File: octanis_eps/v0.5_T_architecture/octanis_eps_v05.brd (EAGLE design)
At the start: 80 x 50 mm, 141 parts, among them IC1 OPA2333DGK, Q3 32.768kHz, Q4 BSS123, U1 BQ24650_RVA_16, U10 CSD16327Q3_DQG_8, U13 CSD16327Q3_DQG_8, U14 CSD16327Q3_DQG_8, U2 Value, U3 Value, U4 Value, U5 TPS2022D, U6 TPS61232, U7 CSD16327Q3_DQG_8, U8 MSP430G2544, U9 CSD16327Q3_DQG_8

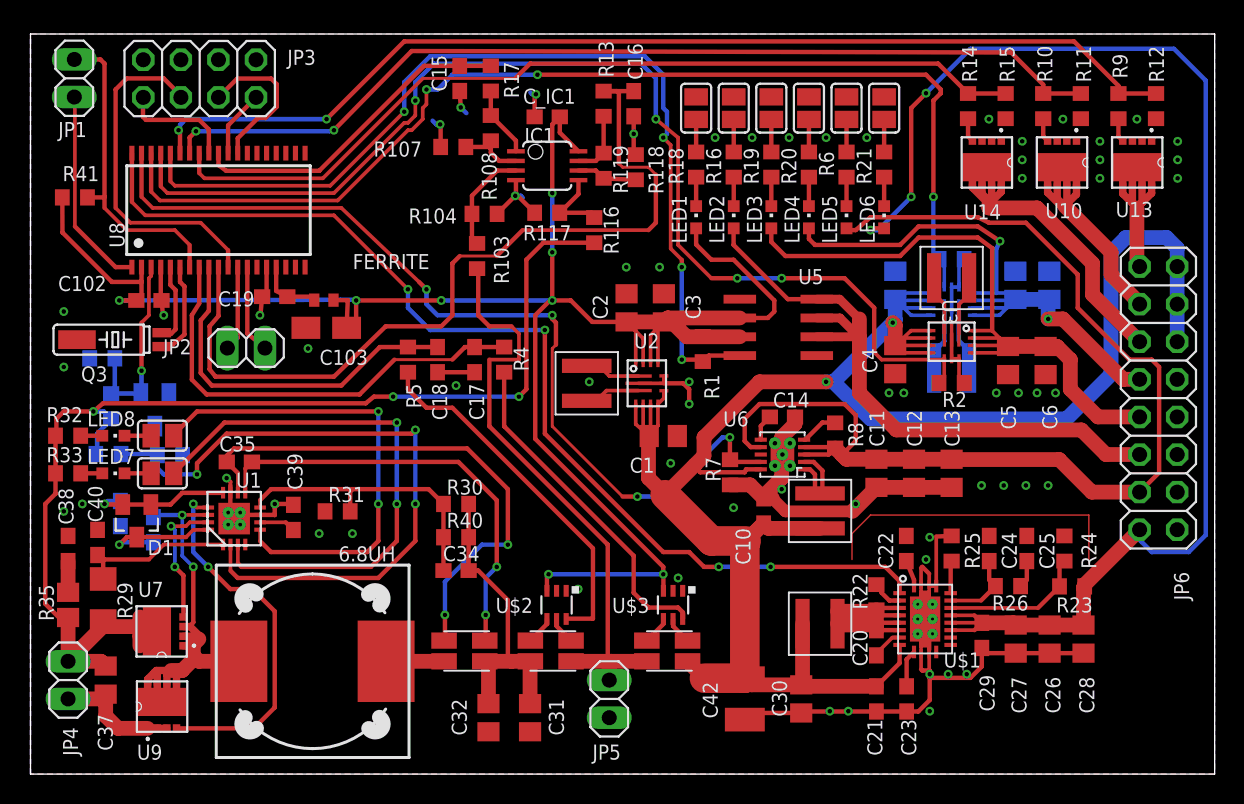
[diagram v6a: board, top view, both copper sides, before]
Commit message: Added mounting holes and header names
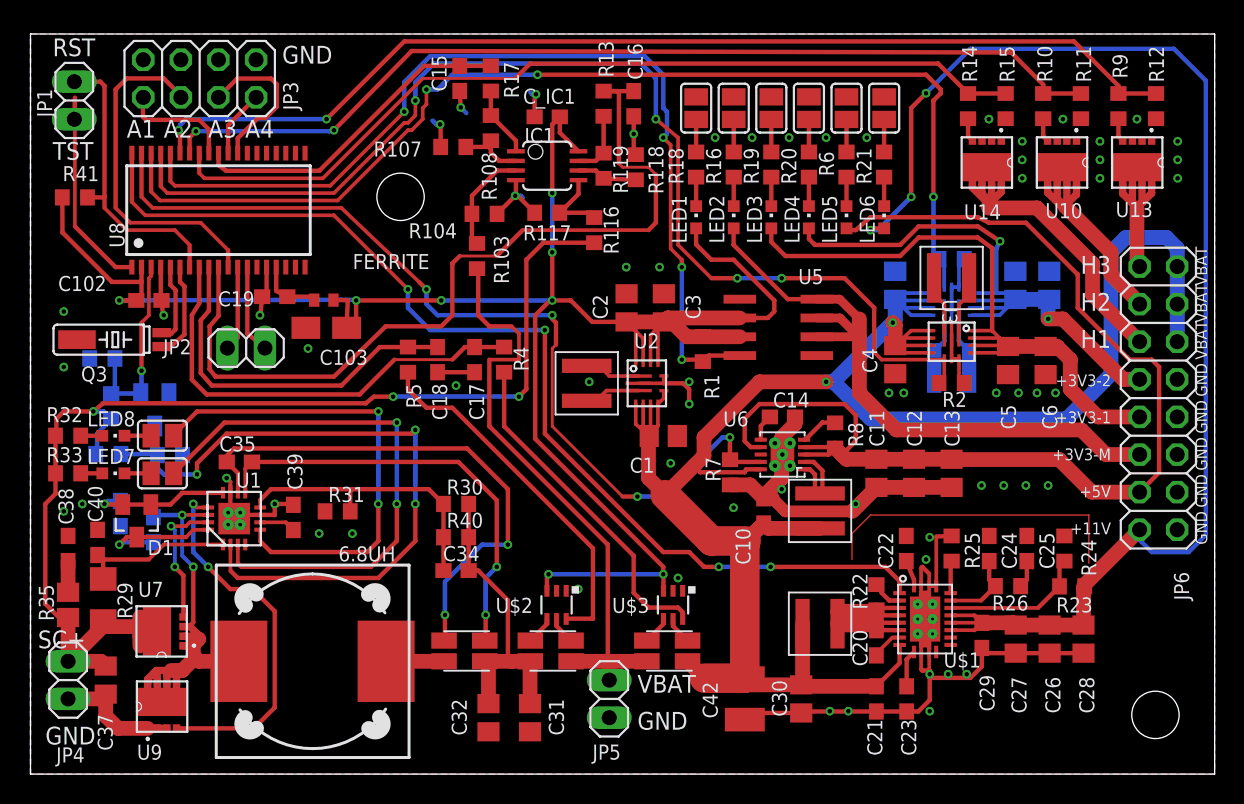
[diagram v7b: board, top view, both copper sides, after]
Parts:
- moved JP1 1.50 mm to (2.96, 45.5)
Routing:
- net N$93: track 21.4 -> 19.9 mm
- net N$75: track 13.7 -> 15.1 mm
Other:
- board text added: "+11V"
- board text added: "+3V3-1"
- board text added: "+3V3-2"
- board text added: "+3V3-M"
- board text added: "+5V"
- board text added: "A1"
- board text added: "A2"
- board text added: "A3"
- board text added: "A4"
- board text added: "GND"
- board text added: "H1"
- board text added: "H2"
- board text added: "H3"
- board text added: "RST"
- board text added: "SC+"
- board text added: "TST"
- board text added: "VBAT"
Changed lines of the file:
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@@
 <setting verticaltext="up"/>
 </settings>
-<grid distance="0.1" unitdist="mm" unit="mm" style="lines" multiple="1" display="no" altdistance="0.025" altunitdist="inch" altunit="inch"/>
+<grid distance="0.5" unitdist="mm" unit="mm" style="lines" multiple="1" display="no" altdistance="0.025" altunitdist="inch" altunit="inch"/>
 <layers>
 <layer number="1" name="Top" color="4" fill="1" visible="yes" active="yes"/>
@@
 <layer number="22" name="bPlace" color="7" fill="1" visible="yes" active="yes"/>
 <layer number="23" name="tOrigins" color="15" fill="1" visible="yes" active="yes"/>
-<layer number="24" name="bOrigins" color="15" fill="1" visible="no" active="yes"/>
+<layer number="24" name="bOrigins" color="15" fill="1" visible="yes" active="yes"/>
 <layer number="25" name="tNames" color="7" fill="1" visible="yes" active="yes"/>
-<layer number="26" name="bNames" color="7" fill="1" visible="no" active="yes"/>
+<layer number="26" name="bNames" color="7" fill="1" visible="yes" active="yes"/>
 <layer number="27" name="tValues" color="7" fill="1" visible="no" active="yes"/>
-<layer number="28" name="bValues" color="7" fill="1" visible="no" active="yes"/>
+<layer number="28" name="bValues" color="7" fill="1" visible="yes" active="yes"/>
 <layer number="29" name="tStop" color="7" fill="3" visible="no" active="yes"/>
 <layer number="30" name="bStop" color="7" fill="6" visible="no" active="yes"/>
@@
 <layer number="42" name="bRestrict" color="1" fill="10" visible="no" active="yes"/>
 <layer number="43" name="vRestrict" color="2" fill="10" visible="no" active="yes"/>
-<layer number="44" name="Drills" color="7" fill="1" visible="no" active="yes"/>
-<layer number="45" name="Holes" color="7" fill="1" visible="no" active="yes"/>
+<layer number="44" name="Drills" color="7" fill="1" visible="yes" active="yes"/>
+<layer number="45" name="Holes" color="7" fill="1" visible="yes" active="yes"/>
 <layer number="46" name="Milling" color="3" fill="1" visible="no" active="yes"/>
 <layer number="47" name="Measures" color="7" fill="1" visible="no" active="yes"/>
@@
 <layer number="50" name="dxf" color="7" fill="1" visible="no" active="no"/>
 <layer number="51" name="tDocu" color="7" fill="1" visible="yes" active="yes"/>
-<layer number="52" name="bDocu" color="7" fill="1" visible="no" active="yes"/>
+<layer number="52" name="bDocu" color="7" fill="1" visible="yes" active="yes"/>
 <layer number="53" name="tGND_GNDA" color="7" fill="9" visible="no" active="no"/>
 <layer number="54" name="bGND_GNDA" color="1" fill="9" visible="no" active="no"/>
@@
 <wire x1="80" y1="50" x2="0" y2="50" width="0" layer="20"/>
 <wire x1="0" y1="50" x2="0" y2="0" width="0" layer="20"/>
+<hole x="25" y="39" drill="3.2"/>
+<hole x="76" y="4" drill="3.2"/>
+<text x="79.5" y="33" size="0.8" layer="25" rot="R90">VBAT</text>
+<text x="79.5" y="30.5" size="0.8" layer="25" rot="R90">VBAT</text>
+<text x="79.5" y="28" size="0.8" layer="25" rot="R90">VBAT</text>
+<text x="79.5" y="25.5" size="0.8" layer="25" rot="R90">GND</text>
+<text x="79.5" y="23" size="0.8" layer="25" rot="R90">GND</text>
+<text x="79.5" y="20.5" size="0.8" layer="25" rot="R90">GND</text>
+<text x="79.5" y="18" size="0.8" layer="25" rot="R90">GND</text>
+<text x="79.5" y="15.5" size="0.8" layer="25" rot="R90">GND</text>
+<text x="73" y="24.5" size="0.8" layer="25" rot="R180">+3V3-1</text>
+<text x="73" y="27" size="0.8" layer="25" rot="R180">+3V3-2</text>
+<text x="73" y="22" size="0.8" layer="25" rot="R180">+3V3-M</text>
+<text x="73" y="19.5" size="0.8" layer="25" rot="R180">+5V</text>
+<text x="73" y="17" size="0.8" layer="25" rot="R180">+11V</text>
+<text x="73" y="30" size="1.2" layer="25" rot="R180">H1</text>
+<text x="73" y="32.5" size="1.2" layer="25" rot="R180">H2</text>
+<text x="73" y="35" size="1.2" layer="25" rot="R180">H3</text>
+<text x="41" y="3" size="1.2" layer="25">GND</text>
+<text x="41" y="5.5" size="1.2" layer="25">VBAT</text>
+<text x="1" y="2" size="1.2" layer="25">GND</text>
+<text x="0.5" y="8.5" size="1.2" layer="25">SC+</text>
+<text x="17" y="48" size="1.2" layer="25">GND</text>
+<text x="6.5" y="43" size="1.2" layer="25">A1</text>
+<text x="9" y="43" size="1.2" layer="25">A2</text>
+<text x="12" y="43" size="1.2" layer="25">A3</text>
+<text x="14.5" y="43" size="1.2" layer="25">A4</text>
+<text x="1.5" y="41.5" size="1.2" layer="25">TST</text>
+<text x="1.5" y="48.5" size="1.2" layer="25">RST</text>
 </plain>
 <attributes>
@@
 </element>
 <element name="R104" library="rcl" package="R0603" value="100k" x="30.674" y="37.849" smashed="yes" rot="R180">
-<attribute name="NAME" x="28.809" y="38.214" size="1.016" layer="25" rot="R180"/>
+<attribute name="NAME" x="28.809" y="37.214" size="1.016" layer="25" rot="R180"/>
 <attribute name="VALUE" x="31.309" y="39.754" size="1.27" layer="27" rot="R180"/>
 </element>
@@
 </element>
 <element name="R24" library="resistor" package="R0603" value="56k" x="69.85" y="15.24" smashed="yes" rot="R270">
-<attribute name="NAME" x="72.015" y="13.875" size="1.016" layer="25" rot="R90"/>
+<attribute name="NAME" x="72.015" y="13.375" size="1.016" layer="25" rot="R90"/>
 <attribute name="VALUE" x="67.945" y="15.875" size="1.27" layer="27" rot="R270"/>
 </element>
@@
 <attribute name="VALUE" x="63.975" y="44.7744" size="1.27" layer="27" ratio="6" rot="SR270"/>
 </element>
-<element name="JP1" library="Headerlibrary" package="1X02" value="" x="2.96" y="47.01" smashed="yes" rot="R270">
-<attribute name="NAME" x="1.8738" y="43.0388" size="1.016" layer="25" ratio="10"/>
-<attribute name="VALUE" x="-0.215" y="49.55" size="1.27" layer="27" rot="R270"/>
+<element name="JP1" library="Headerlibrary" package="1X02" value="" x="2.96" y="45.51" smashed="yes" rot="R270">
+<attribute name="NAME" x="1.4612" y="44.3738" size="1.016" layer="25" ratio="10" rot="R90"/>
+<attribute name="VALUE" x="-0.215" y="48.05" size="1.27" layer="27" rot="R270"/>
 </element>
 <element name="R41" library="rcl" package="R0603" value="10k" x="3" y="38.96" smashed="yes" rot="R180">
@@
 </element>
 <element name="JP3" library="Headerlibrary" package="2X04" value="" x="11.43" y="46.99" smashed="yes">
-<attribute name="NAME" x="17.35" y="47.915" size="1.016" layer="25" ratio="10"/>
+<attribute name="NAME" x="18.085" y="44.85" size="1.016" layer="25" ratio="10" rot="R90"/>
 <attribute name="VALUE" x="6.35" y="42.545" size="1.27" layer="27"/>
 </element>
@@
 </element>
 <element name="JP4" library="Headerlibrary" package="1X02" value="" x="2.54" y="6.35" smashed="yes" rot="R90">
-<attribute name="NAME" x="3.2112" y="1.2338" size="1.016" layer="25" ratio="10" rot="R90"/>
+<attribute name="NAME" x="1.7338" y="0.7888" size="1.016" layer="25" ratio="10"/>
 <attribute name="VALUE" x="5.715" y="3.81" size="1.27" layer="27" rot="R90"/>
 </element>
@@
 <wire x1="5.75" y1="34.25" x2="3" y2="37" width="0.3" layer="1"/>
 <wire x1="3" y1="37" x2="3" y2="45.7" width="0.25" layer="1"/>
-<wire x1="3" y1="45.7" x2="2.96" y2="45.74" width="0.3" layer="1"/>
+<wire x1="3" y1="45.7" x2="2.96" y2="44.24" width="0.3" layer="1"/>
 </signal>
 <signal name="N$93">
@@
 <contactref element="JP1" pad="1"/>
 <contactref element="R41" pad="1"/>
-<wire x1="2.96" y1="48.28" x2="4.72" y2="48.28" width="0.3" layer="1"/>
-<wire x1="4.72" y1="48.28" x2="5" y2="48" width="0.3" layer="1"/>
-<wire x1="5" y1="48" x2="5" y2="39" width="0.3" layer="1"/>
+<wire x1="2.96" y1="46.78" x2="4.72" y2="46.78" width="0.3" layer="1"/>
+<wire x1="4.72" y1="46.78" x2="5" y2="46.5" width="0.3" layer="1"/>
+<wire x1="5" y1="46.5" x2="5" y2="39" width="0.3" layer="1"/>
 <wire x1="5" y1="39" x2="5" y2="38.25" width="0.3" layer="1"/>
 <wire x1="5" y1="38.25" x2="6.5" y2="36.75" width="0.25" layer="1"/>

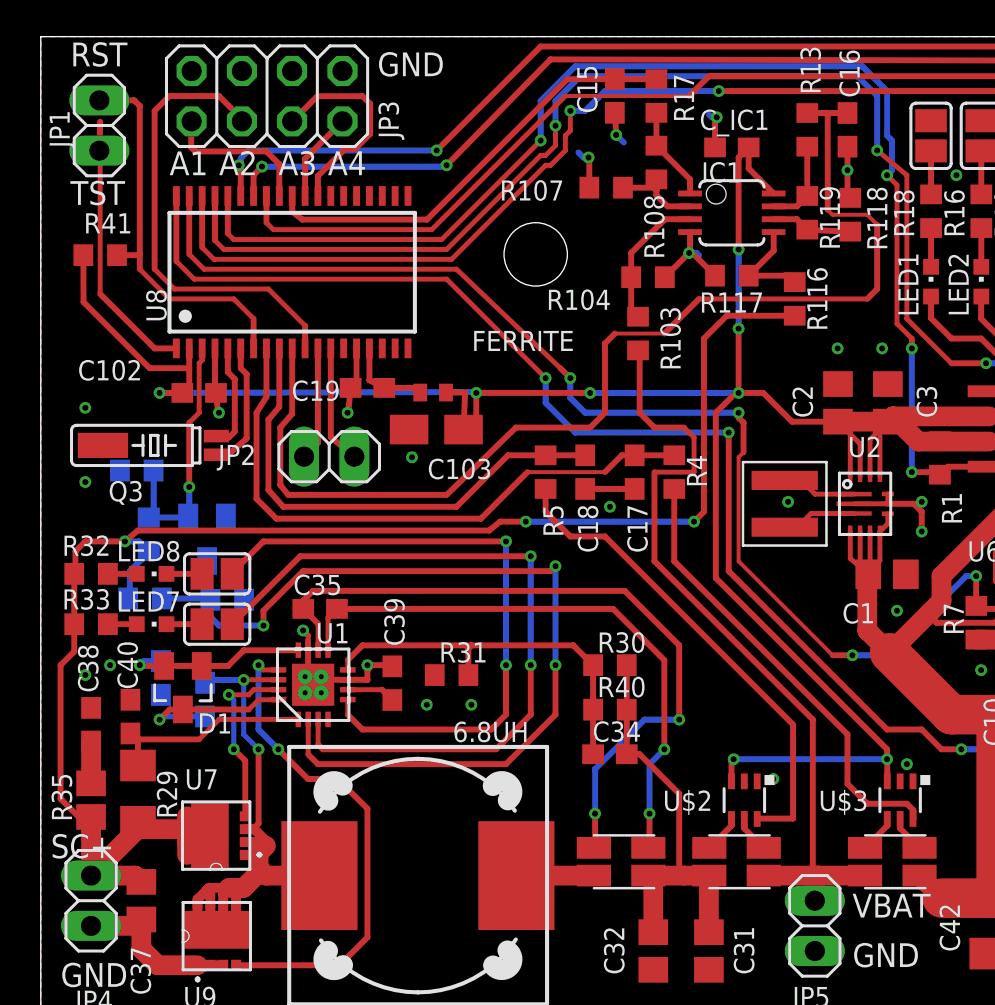
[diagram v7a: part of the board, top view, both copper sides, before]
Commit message: minor eps changes. stencil laser cut files for v0.6 added
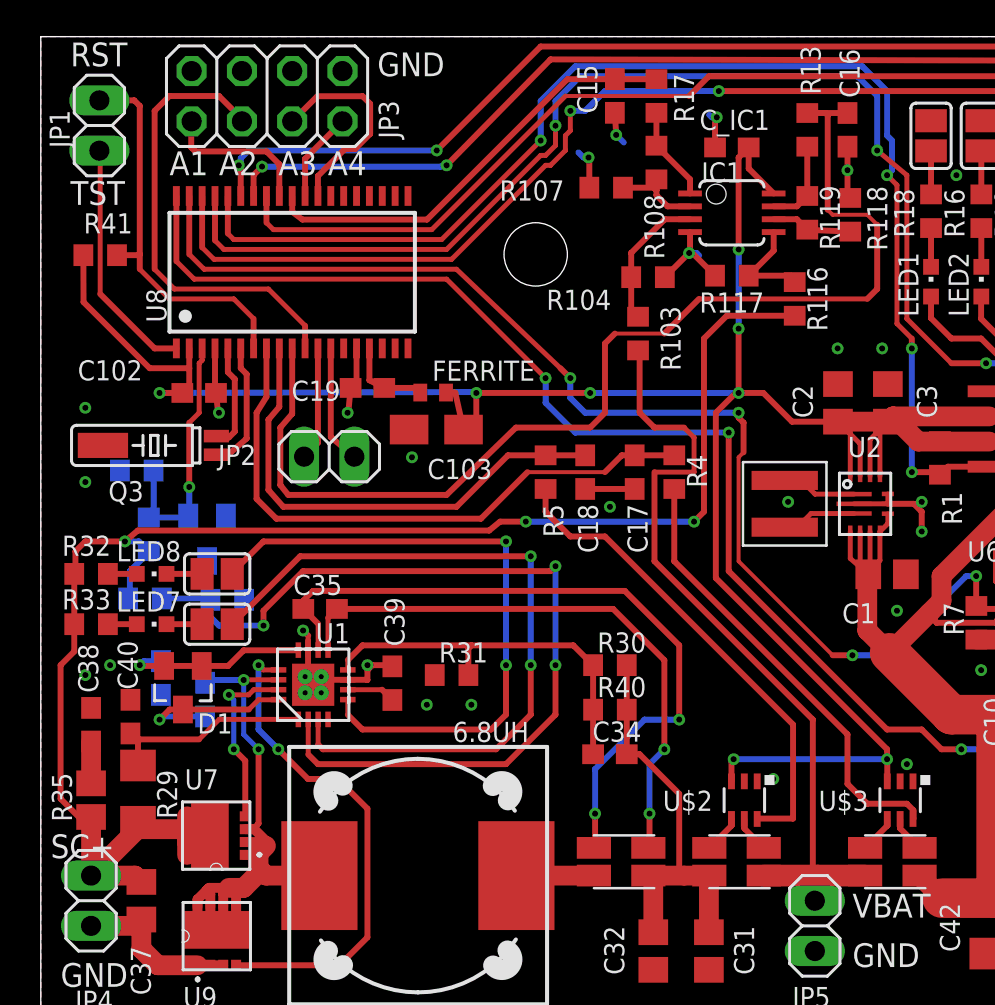
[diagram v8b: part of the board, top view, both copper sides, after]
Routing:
- net N$75: track 15.1 -> 12.2 mm
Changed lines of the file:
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@@
 <?xml version="1.0" encoding="utf-8"?>
 <!DOCTYPE eagle SYSTEM "eagle.dtd">
-<eagle version="7.5.0">
+<eagle version="7.2.0">
 <drawing>
 <settings>
@@
 <setting verticaltext="up"/>
 </settings>
-<grid distance="0.5" unitdist="mm" unit="mm" style="lines" multiple="1" display="no" altdistance="0.025" altunitdist="inch" altunit="inch"/>
+<grid distance="0.5" unitdist="mm" unit="inch" style="lines" multiple="1" display="no" altdistance="0.025" altunitdist="inch" altunit="inch"/>
 <layers>
 <layer number="1" name="Top" color="4" fill="1" visible="yes" active="yes"/>
@@
 <layer number="26" name="bNames" color="7" fill="1" visible="yes" active="yes"/>
 <layer number="27" name="tValues" color="7" fill="1" visible="no" active="yes"/>
-<layer number="28" name="bValues" color="7" fill="1" visible="yes" active="yes"/>
+<layer number="28" name="bValues" color="7" fill="1" visible="no" active="yes"/>
 <layer number="29" name="tStop" color="7" fill="3" visible="no" active="yes"/>
 <layer number="30" name="bStop" color="7" fill="6" visible="no" active="yes"/>
@@
 <layer number="42" name="bRestrict" color="1" fill="10" visible="no" active="yes"/>
 <layer number="43" name="vRestrict" color="2" fill="10" visible="no" active="yes"/>
-<layer number="44" name="Drills" color="7" fill="1" visible="yes" active="yes"/>
-<layer number="45" name="Holes" color="7" fill="1" visible="yes" active="yes"/>
+<layer number="44" name="Drills" color="7" fill="1" visible="no" active="yes"/>
+<layer number="45" name="Holes" color="7" fill="1" visible="no" active="yes"/>
 <layer number="46" name="Milling" color="3" fill="1" visible="no" active="yes"/>
 <layer number="47" name="Measures" color="7" fill="1" visible="no" active="yes"/>
@@
 <layer number="49" name="Reference" color="7" fill="1" visible="no" active="yes"/>
 <layer number="50" name="dxf" color="7" fill="1" visible="no" active="no"/>
-<layer number="51" name="tDocu" color="7" fill="1" visible="yes" active="yes"/>
-<layer number="52" name="bDocu" color="7" fill="1" visible="yes" active="yes"/>
+<layer number="51" name="tDocu" color="7" fill="1" visible="no" active="yes"/>
+<layer number="52" name="bDocu" color="7" fill="1" visible="no" active="yes"/>
 <layer number="53" name="tGND_GNDA" color="7" fill="9" visible="no" active="no"/>
 <layer number="54" name="bGND_GNDA" color="1" fill="9" visible="no" active="no"/>
@@
 </element>
 <element name="FERRITE" library="inductors" package="0402" value="100mH" x="19.82" y="32.02" smashed="yes" rot="R180">
-<attribute name="NAME" x="26.955" y="35.135" size="1.016" layer="25" rot="R180"/>
+<attribute name="NAME" x="24.955" y="33.635" size="1.016" layer="25" rot="R180"/>
 <attribute name="VALUE" x="20.455" y="33.925" size="1.27" layer="27" rot="R180"/>
 </element>
@@
 <wire x1="6.85" y1="34.25" x2="5.75" y2="34.25" width="0.3" layer="1"/>
 <wire x1="5.75" y1="34.25" x2="3" y2="37" width="0.3" layer="1"/>
-<wire x1="3" y1="37" x2="3" y2="45.7" width="0.25" layer="1"/>
-<wire x1="3" y1="45.7" x2="2.96" y2="44.24" width="0.3" layer="1"/>
+<wire x1="3" y1="37" x2="3" y2="44.2" width="0.25" layer="1"/>
+<wire x1="3" y1="44.2" x2="2.96" y2="44.24" width="0.3" layer="1"/>
 </signal>
 <signal name="N$93">
@@
 <wire x1="4.96" y1="24.5" x2="5.45" y2="24.01" width="0.3" layer="16"/>
 <wire x1="4.91" y1="10.338" x2="4.91" y2="9.99" width="0.3" layer="1"/>
-<wire x1="4.91" y1="9.99" x2="2.54" y2="7.62" width="0.3" layer="1"/>
+<wire x1="4.91" y1="9.99" x2="4.88499375" y2="9.96499375" width="0.3" layer="1"/>
+<wire x1="4.88499375" y1="9.96499375" x2="2.54" y2="7.62" width="0.3" layer="1"/>
 <wire x1="7.39" y1="10.615003125" x2="7.39" y2="9.96499375" width="1" layer="1"/>
 <wire x1="7.39" y1="9.96499375" x2="7.39" y2="9.31500625" width="1" layer="1"/>
@@
 <contactref element="R_SENSE1" pad="I1"/>
 <contactref element="R103" pad="2"/>
-<wire x1="36.52081875" y1="7.62" x2="39.25" y2="7.62" width="1" layer="1"/>
-<wire x1="39.25" y1="7.62" x2="41.64" y2="7.62" width="1" layer="1"/>
+<wire x1="36.52081875" y1="7.62" x2="39.25" y2="7.62" width="1.1" layer="1"/>
+<wire x1="39.25" y1="7.62" x2="41.64" y2="7.62" width="1.1" layer="1"/>
 <wire x1="39.1" y1="6.35" x2="39.1" y2="7.47" width="1" layer="1"/>
 <wire x1="39.1" y1="7.47" x2="39.25" y2="7.62" width="1" layer="1"/>
@@
 <wire x1="2.16" y1="36.59" x2="5.5" y2="33.25" width="0.3" layer="1"/>
 <wire x1="5.5" y1="33.25" x2="7.5" y2="33.25" width="0.3" layer="1"/>
-<wire x1="20.47" y1="32.02" x2="21.435" y2="32.02" width="0.3" layer="1"/>
-<wire x1="21.435" y1="32.02" x2="21.355" y2="30.15" width="0.3" layer="1"/>
+<wire x1="20.47" y1="32.02" x2="20.935" y2="32.02" width="0.3" layer="1"/>
+<wire x1="20.935" y1="32.02" x2="21.355" y2="30.15" width="0.3" layer="1"/>
 <via x="6" y="32" extent="1-16" drill="0.3"/>
 <wire x1="6" y1="32" x2="7.15" y2="32" width="0.3" layer="1"/>
